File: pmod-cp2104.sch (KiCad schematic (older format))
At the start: 36 parts, among them P1 PMOD-CONN_6X2

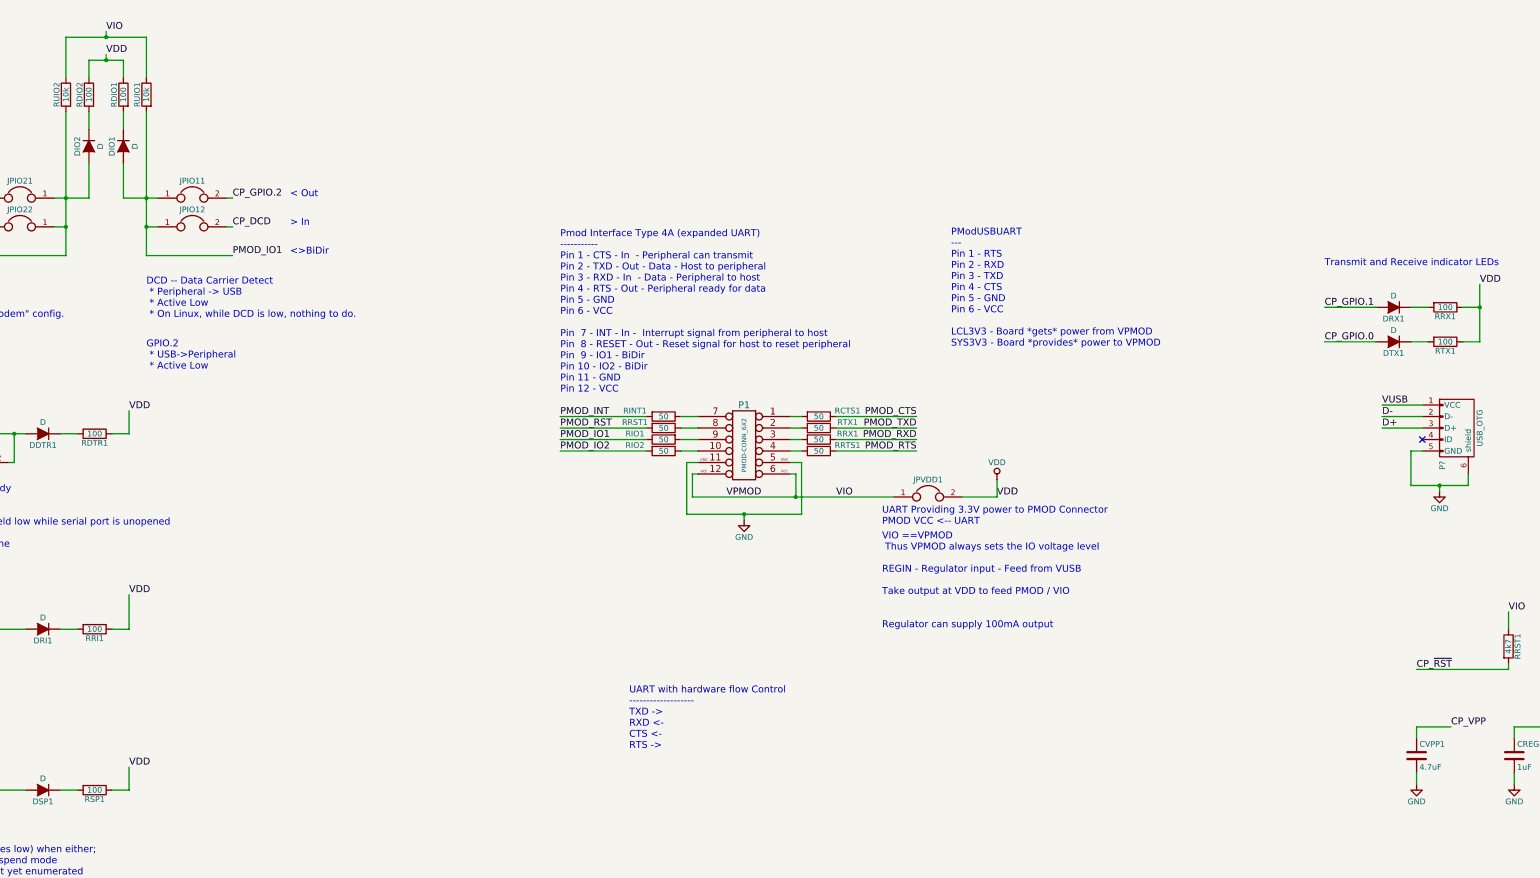
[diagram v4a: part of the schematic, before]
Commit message: Change LED resistor to be value "LEDO"
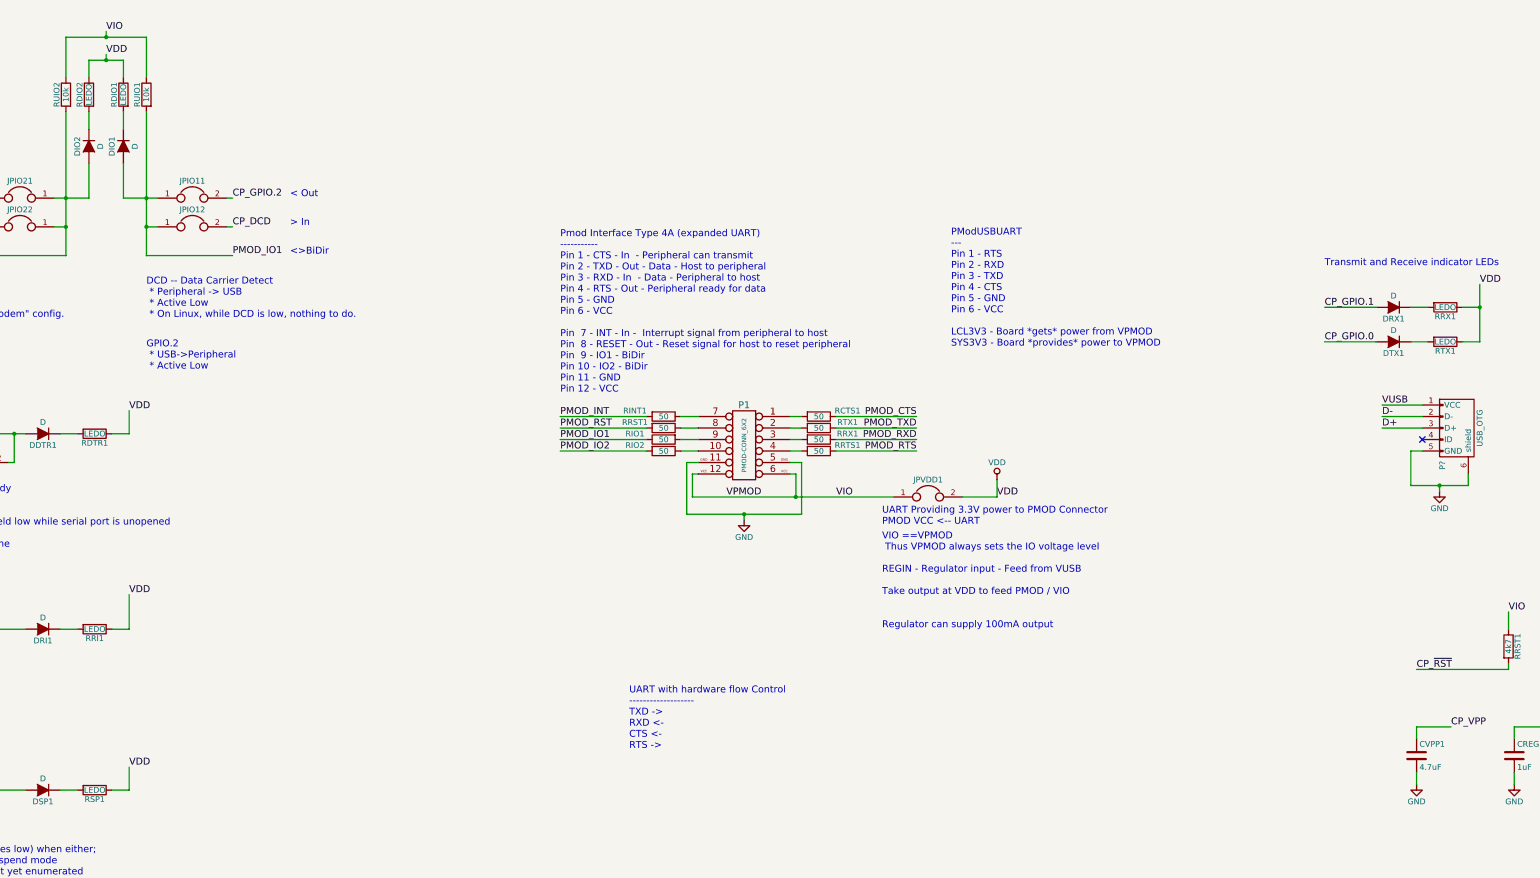
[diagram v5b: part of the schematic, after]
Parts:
- RDIO1, RDIO2, RDTR1, RRI1, RRX1, RSP1, RTX1: value 100 -> LEDO
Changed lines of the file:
@@
 P 8300 1250
 F 0 "RRX1" V 8380 1250 50  0000 C CNN
-F 1 "100" V 8300 1250 50  0000 C CNN
+F 1 "LEDO" V 8300 1250 50  0000 C CNN
 F 2 "" V 8230 1250 50  0000 C CNN
 F 3 "" H 8300 1250 50  0000 C CNN
@@
 P 8300 1550
 F 0 "RTX1" V 8380 1550 50  0000 C CNN
-F 1 "100" V 8300 1550 50  0000 C CNN
+F 1 "LEDO" V 8300 1550 50  0000 C CNN
 F 2 "" V 8230 1550 50  0000 C CNN
 F 3 "" H 8300 1550 50  0000 C CNN
@@
 P -3450 2350
 F 0 "RDTR1" V -3370 2350 50  0000 C CNN
-F 1 "100" V -3450 2350 50  0000 C CNN
+F 1 "LEDO" V -3450 2350 50  0000 C CNN
 F 2 "" V -3520 2350 50  0000 C CNN
 F 3 "" H -3450 2350 50  0000 C CNN
@@
 P -3450 4050
 F 0 "RRI1" V -3370 4050 50  0000 C CNN
-F 1 "100" V -3450 4050 50  0000 C CNN
+F 1 "LEDO" V -3450 4050 50  0000 C CNN
 F 2 "" V -3520 4050 50  0000 C CNN
 F 3 "" H -3450 4050 50  0000 C CNN
@@
 P -3200 -600
 F 0 "RDIO1" V -3120 -600 50  0000 C CNN
-F 1 "100" V -3200 -600 50  0000 C CNN
+F 1 "LEDO" V -3200 -600 50  0000 C CNN
 F 2 "" V -3270 -600 50  0000 C CNN
 F 3 "" H -3200 -600 50  0000 C CNN
@@
 P -3500 -600
 F 0 "RDIO2" V -3420 -600 50  0000 C CNN
-F 1 "100" V -3500 -600 50  0000 C CNN
+F 1 "LEDO" V -3500 -600 50  0000 C CNN
 F 2 "" V -3570 -600 50  0000 C CNN
 F 3 "" H -3500 -600 50  0000 C CNN
@@
 P -3450 5450
 F 0 "RSP1" V -3370 5450 50  0000 C CNN
-F 1 "100" V -3450 5450 50  0000 C CNN
+F 1 "LEDO" V -3450 5450 50  0000 C CNN
 F 2 "" V -3520 5450 50  0000 C CNN
 F 3 "" H -3450 5450 50  0000 C CNN

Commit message: Slowly starting to connect everything together.
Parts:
- added U1: CP2104, symbol CP2104
- gave numbers to parts that had none: 1
- renumbered RDTR1 to RDDTR1, RRI1 to RDRI1, RRX1 to RDRX1, RSP1 to RDSP1, RTX1 to RDTX1, RRST1 to RURST1, RDSP1 to RUSP1
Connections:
- net CP_DCD: now also U1.24 (DCD)
- net CP_DSR: now also U1.22 (DSR)
- net CP_DTR: now also U1.23 (DTR)
- net CP_GPIO.0: now also U1.14 (GPIO.0)
- net CP_GPIO.1: now also U1.13 (GPIO.1)
- net CP_GPIO.2: now also U1.12 (GPIO.2)
- net CP_GPIO.3: now also U1.11 (GPIO.3)
- net CP_REGIN: now also U1.7 (REGIN)
- net CP_RI: now also U1.1 (RI)
- net CP_VPP: now also U1.16 (VPP)
- net CP_~RST: now also U1.9 (~RST)
- net CP_~SUSPEND~: now also U1.15 (~SUSPEND)
- net D+: now also U1.3 (D+)
- net D-: now also U1.4 (D-)
- net GND: now also U1.2 (GND)
- net PMOD_CTS: now also U1.18 (CTS)
- net PMOD_RTS: now also U1.19 (RTS)
- net PMOD_RXD: now also U1.20 (RXD)
- net PMOD_TXD: now also U1.21 (TXD)
- net VIO: now also U1.5 (VIO)
- net VUSB: now also U1.8 (VBUS)
- no-connect marks 1 -> 3
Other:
- moved on the sheet: CREGIN1, CVPP1, DDTR1, DIO1, DIO2, DRI1, DRX1, DSP1, DTX1, JPDTR1, JPIO11, JPIO12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

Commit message: Adding footprints for everything.
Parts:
- CREGIN1, CVPP1: footprint (none) -> Capacitors_SMD:C_0805
- DDTR1, DIO1, DIO2, DRI1, DRX1, DSP1, DTX1: footprint (none) -> Diodes_SMD:D_0603
- JPDTR1, JPIO11, JPIO12, JPIO21, JPIO22, JPVDD1: footprint (none) -> Pin_Headers:Pin_Header_Straight_1x02
- P1: footprint (none) -> Pin_Headers:Pin_Header_Angled_2x06
- P2: footprint (none) -> Connect:USB_Mini-B
- RCTS1, RDDTR1, RDIO1, RDIO2, RDRI1, RDRX1, RDSP1, RDTX1, RINT1, RIO1, RIO2, RRST1, RRTS1, RRX1, RTX1, RUIO1, RUIO2, RURST1, RUSP1: footprint (none) -> Resistors_SMD:R_0402
- U1: footprint (none) -> Housings_DFN_QFN:QFN-24_4x4mm_Pitch0.5mm

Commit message: Fixing for parts I already have.
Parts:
- DDTR1, DIO1, DIO2, DRI1, DRX1, DSP1, DTX1: footprint Diodes_SMD:D_0603 -> LEDs:LED_0402
- RCTS1, RDDTR1, RDIO1, RDIO2, RDRI1, RDRX1, RDSP1, RDTX1, RINT1, RIO1, RIO2, RRST1, RRTS1, RRX1, RTX1, RUIO1, RUIO2, RURST1, RUSP1: footprint Resistors_SMD:R_0402 -> Resistors_SMD:R_0603
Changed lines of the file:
@@
 F 0 "DTX1" H 2500 5300 50  0000 C CNN
 F 1 "D" H 2500 5100 50  0001 C CNN
-F 2 "Diodes_SMD:D_0603" H 2500 5200 50  0001 C CNN
+F 2 "LEDs:LED_0402" H 2500 5200 50  0001 C CNN
 F 3 "" H 2500 5200 50  0000 C CNN
 	1    2500 5200
@@
 F 0 "DRX1" H 2500 5100 50  0000 C CNN
 F 1 "D" H 2500 4900 50  0001 C CNN
-F 2 "Diodes_SMD:D_0603" H 2500 5000 50  0001 C CNN
+F 2 "LEDs:LED_0402" H 2500 5000 50  0001 C CNN
 F 3 "" H 2500 5000 50  0000 C CNN
 	1    2500 5000
@@
 F 0 "RURST1" V 5700 3850 50  0000 C CNN
 F 1 "4k7" V 5800 3850 50  0000 C CNN
-F 2 "Resistors_SMD:R_0402" V 5730 3850 50  0001 C CNN
+F 2 "Resistors_SMD:R_0603" V 5730 3850 50  0001 C CNN
 F 3 "" H 5800 3850 50  0000 C CNN
 	1    5800 3850
@@
 F 0 "RDRX1" V 2130 5000 50  0000 C CNN
 F 1 "LEDO" V 2050 5000 50  0000 C CNN
-F 2 "Resistors_SMD:R_0402" V 1980 5000 50  0001 C CNN
+F 2 "Resistors_SMD:R_0603" V 1980 5000 50  0001 C CNN
 F 3 "" H 2050 5000 50  0000 C CNN
 	1    2050 5000
@@
 F 0 "RDTX1" V 2130 5200 50  0000 C CNN
 F 1 "LEDO" V 2050 5200 50  0000 C CNN
-F 2 "Resistors_SMD:R_0402" V 1980 5200 50  0001 C CNN
+F 2 "Resistors_SMD:R_0603" V 1980 5200 50  0001 C CNN
 F 3 "" H 2050 5200 50  0000 C CNN
 	1    2050 5200
@@
 F 0 "DDTR1" H 16450 4250 50  0000 C CNN
 F 1 "D" H 16450 4050 50  0000 C CNN
-F 2 "Diodes_SMD:D_0603" H 16450 4150 50  0001 C CNN
+F 2 "LEDs:LED_0402" H 16450 4150 50  0001 C CNN
 F 3 "" H 16450 4150 50  0000 C CNN
 	1    16450 4150
@@
 F 0 "RDDTR1" V 16980 4150 50  0000 C CNN
 F 1 "LEDO" V 16900 4150 50  0000 C CNN
-F 2 "Resistors_SMD:R_0402" V 16830 4150 50  0001 C CNN
+F 2 "Resistors_SMD:R_0603" V 16830 4150 50  0001 C CNN
 F 3 "" H 16900 4150 50  0000 C CNN
 	1    16900 4150
@@
 F 0 "DRI1" H 16450 5950 50  0000 C CNN
 F 1 "D" H 16450 5750 50  0000 C CNN
-F 2 "Diodes_SMD:D_0603" H 16450 5850 50  0001 C CNN
+F 2 "LEDs:LED_0402" H 16450 5850 50  0001 C CNN
 F 3 "" H 16450 5850 50  0000 C CNN
 	1    16450 5850
@@
 F 0 "RDRI1" V 16980 5850 50  0000 C CNN
 F 1 "LEDO" V 16900 5850 50  0000 C CNN
-F 2 "Resistors_SMD:R_0402" V 16830 5850 50  0001 C CNN
+F 2 "Resistors_SMD:R_0603" V 16830 5850 50  0001 C CNN
 F 3 "" H 16900 5850 50  0000 C CNN
 	1    16900 5850
@@
 F 0 "RINT1" V 1450 1950 50  0000 C CNN
 F 1 "50" V 1500 2200 50  0000 C CNN
-F 2 "Resistors_SMD:R_0402" V 1430 2200 50  0001 C CNN
+F 2 "Resistors_SMD:R_0603" V 1430 2200 50  0001 C CNN
 F 3 "" H 1500 2200 50  0000 C CNN
 	1    1500 2200
@@
 F 0 "DIO2" H 16850 1750 50  0000 C CNN
 F 1 "D" H 16850 1550 50  0000 C CNN
-F 2 "Diodes_SMD:D_0603" H 16850 1650 50  0001 C CNN
+F 2 "LEDs:LED_0402" H 16850 1650 50  0001 C CNN
 F 3 "" H 16850 1650 50  0000 C CNN
 	1    16850 1650
@@
 F 0 "DIO1" H 17150 1750 50  0000 C CNN
 F 1 "D" H 17150 1550 50  0000 C CNN
-F 2 "Diodes_SMD:D_0603" H 17150 1650 50  0001 C CNN
+F 2 "LEDs:LED_0402" H 17150 1650 50  0001 C CNN
 F 3 "" H 17150 1650 50  0000 C CNN
 	1    17150 1650
@@
 F 0 "RDIO1" V 17230 1200 50  0000 C CNN
 F 1 "LEDO" V 17150 1200 50  0000 C CNN
-F 2 "Resistors_SMD:R_0402" V 17080 1200 50  0001 C CNN
+F 2 "Resistors_SMD:R_0603" V 17080 1200 50  0001 C CNN
 F 3 "" H 17150 1200 50  0000 C CNN
 	1    17150 1200
@@
 F 0 "RDIO2" V 16930 1200 50  0000 C CNN
 F 1 "LEDO" V 16850 1200 50  0000 C CNN
-F 2 "Resistors_SMD:R_0402" V 16780 1200 50  0001 C CNN
+F 2 "Resistors_SMD:R_0603" V 16780 1200 50  0001 C CNN
 F 3 "" H 16850 1200 50  0000 C CNN
 	1    16850 1200
@@
 F 0 "RUIO1" V 17430 1200 50  0000 C CNN
 F 1 "10k" V 17350 1200 50  0000 C CNN
-F 2 "Resistors_SMD:R_0402" V 17280 1200 50  0001 C CNN
+F 2 "Resistors_SMD:R_0603" V 17280 1200 50  0001 C CNN
 F 3 "" H 17350 1200 50  0000 C CNN
 	1    17350 1200
@@
 F 0 "RUIO2" V 16730 1200 50  0000 C CNN
 F 1 "10k" V 16650 1200 50  0000 C CNN
-F 2 "Resistors_SMD:R_0402" V 16580 1200 50  0001 C CNN
+F 2 "Resistors_SMD:R_0603" V 16580 1200 50  0001 C CNN
 F 3 "" H 16650 1200 50  0000 C CNN
 	1    16650 1200
@@
 F 0 "RRST1" V 1450 2050 50  0000 C CNN
 F 1 "50" V 1500 2300 50  0000 C CNN
-F 2 "Resistors_SMD:R_0402" V 1430 2300 50  0001 C CNN
+F 2 "Resistors_SMD:R_0603" V 1430 2300 50  0001 C CNN
 F 3 "" H 1500 2300 50  0000 C CNN
 	1    1500 2300
@@
 F 0 "RIO2" V 1450 2250 50  0000 C CNN
 F 1 "50" V 1500 2500 50  0000 C CNN
-F 2 "Resistors_SMD:R_0402" V 1430 2500 50  0001 C CNN
+F 2 "Resistors_SMD:R_0603" V 1430 2500 50  0001 C CNN
 F 3 "" H 1500 2500 50  0000 C CNN
 	1    1500 2500
@@
 F 0 "RTX1" V 2800 2550 50  0000 C CNN
 F 1 "50" V 2850 2300 50  0000 C CNN
-F 2 "Resistors_SMD:R_0402" V 2780 2300 50  0001 C CNN
+F 2 "Resistors_SMD:R_0603" V 2780 2300 50  0001 C CNN
 F 3 "" H 2850 2300 50  0000 C CNN
 	1    2850 2300
@@
 F 0 "RRX1" V 2800 2650 50  0000 C CNN
 F 1 "50" V 2850 2400 50  0000 C CNN
-F 2 "Resistors_SMD:R_0402" V 2780 2400 50  0001 C CNN
+F 2 "Resistors_SMD:R_0603" V 2780 2400 50  0001 C CNN
 F 3 "" H 2850 2400 50  0000 C CNN
 	1    2850 2400
@@
 F 0 "RCTS1" V 2800 2450 50  0000 C CNN
 F 1 "50" V 2850 2200 50  0000 C CNN
-F 2 "Resistors_SMD:R_0402" V 2780 2200 50  0001 C CNN
+F 2 "Resistors_SMD:R_0603" V 2780 2200 50  0001 C CNN
 F 3 "" H 2850 2200 50  0000 C CNN
 	1    2850 2200
@@
 F 0 "RRTS1" V 2800 2750 50  0000 C CNN
 F 1 "50" V 2850 2500 50  0000 C CNN
-F 2 "Resistors_SMD:R_0402" V 2780 2500 50  0001 C CNN
+F 2 "Resistors_SMD:R_0603" V 2780 2500 50  0001 C CNN
 F 3 "" H 2850 2500 50  0000 C CNN
 	1    2850 2500
@@
 F 0 "DSP1" H 2500 5700 50  0000 C CNN
 F 1 "D" H 2500 5500 50  0000 C CNN
-F 2 "Diodes_SMD:D_0603" H 2500 5600 50  0001 C CNN
+F 2 "LEDs:LED_0402" H 2500 5600 50  0001 C CNN
 F 3 "" H 2500 5600 50  0000 C CNN
 	1    2500 5600
@@
 F 0 "RDSP1" V 2130 5600 50  0000 C CNN
 F 1 "LEDO" V 2050 5600 50  0000 C CNN
-F 2 "Resistors_SMD:R_0402" V 1980 5600 50  0001 C CNN
+F 2 "Resistors_SMD:R_0603" V 1980 5600 50  0001 C CNN
 F 3 "" H 2050 5600 50  0000 C CNN
 	1    2050 5600
@@
 F 0 "RUSP1" V 3630 5300 50  0000 C CNN
 F 1 "10k" V 3550 5300 50  0000 C CNN
-F 2 "Resistors_SMD:R_0402" V 3480 5300 50  0001 C CNN
+F 2 "Resistors_SMD:R_0603" V 3480 5300 50  0001 C CNN
 F 3 "" H 3550 5300 50  0000 C CNN
 	1    3550 5300
@@
 F 0 "RIO1" V 1450 2650 50  0000 C CNN
 F 1 "50" V 1500 2400 50  0000 C CNN
-F 2 "Resistors_SMD:R_0402" V 1430 2400 50  0001 C CNN
+F 2 "Resistors_SMD:R_0603" V 1430 2400 50  0001 C CNN
 F 3 "" H 1500 2400 50  0000 C CNN
 	1    1500 2400
